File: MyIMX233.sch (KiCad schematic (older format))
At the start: 79 parts, among them IC1 iMX233, IC2 DDR_SDRAM_MT46_x16, J1 USB_OTG, P1 P4v2, P2 1v2, P3 VDDA1v8, P4 2v5, P5 3v3, P6 P4v2, SW1 SWITCH_PUSHBUTTON, Y1 24Mhz

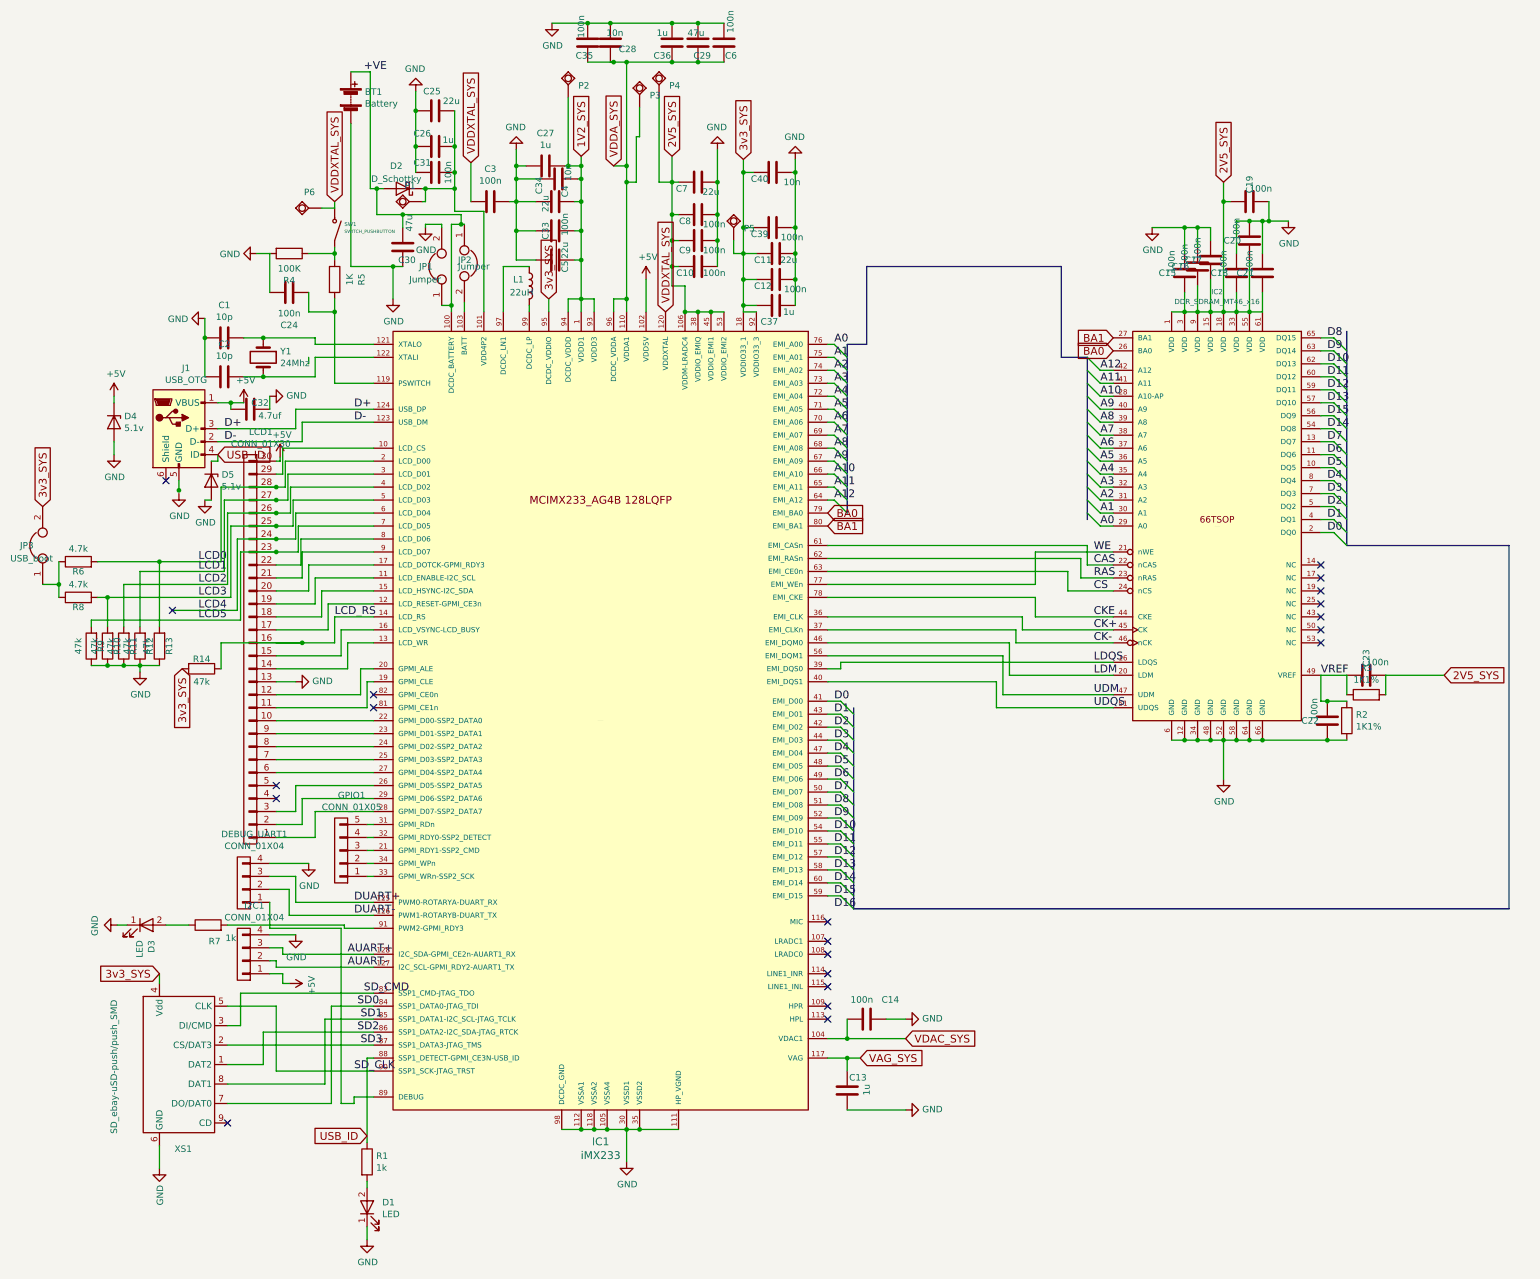
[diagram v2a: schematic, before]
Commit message: added boot resistors and 2.5v_VDDM is separated for ram, new battery connections with resistors for non battery mode
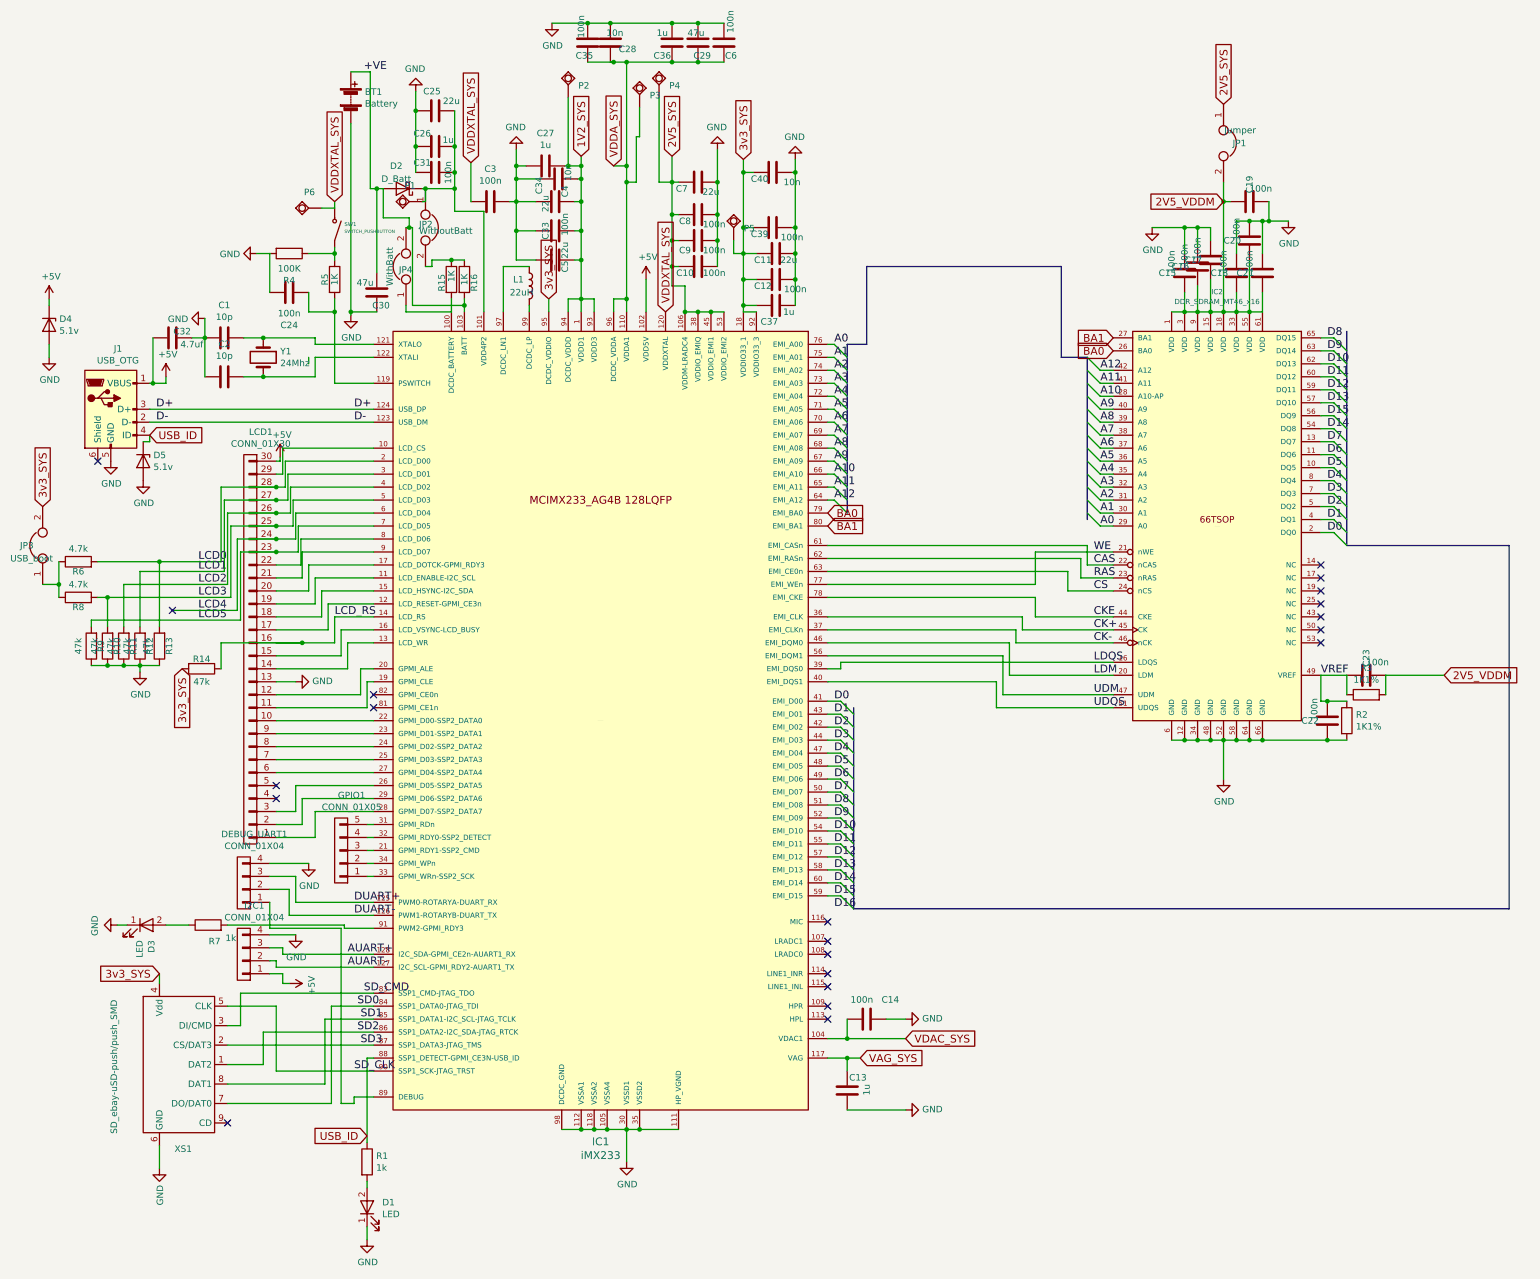
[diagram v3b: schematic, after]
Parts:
- added JP4: WithBatt, Pin_Headers:Pin_Header_Straight_1x02_Pitch2.54mm, symbol Jumper
- added R15, R16: 1K, Resistors_SMD:R_0603, symbol R
- D2: value D_Schottky -> D_Batt
- JP2: value Jumper -> WithoutBatt
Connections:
- net +VE: now also IC1.103 (BATT), JP4.2, R16.2; no longer IC1.100 (DCDC_BATTERY), JP1.1, JP2.1
- net 2V5_SYS: now also JP1.1; no longer C15.1, C16.1, C17.1, C18.1, C19.1, C20.1, C21.1, C23.2, IC2.1 (VDD), IC2.15 (VDD), IC2.18 (VDD), IC2.3 (VDD), IC2.33 (VDD), IC2.55 (VDD), IC2.61 (VDD), IC2.9 (VDD), R3.2
- net GND: now also J1.5 (GND); no longer JP1.2
- net at C25.2, C26.2, C31.1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: now also JP2.1
- net at JP2.2: now also R15.1, R16.1; no longer IC1.103 (BATT)
- new net: IC1.100 (DCDC_BATTERY), JP4.1, R15.2
- new net 2V5_VDDM: C15.1, C16.1, C17.1, C18.1, C19.1, C20.1, C21.1, C23.2, IC2.1 (VDD), IC2.15 (VDD), IC2.18 (VDD), IC2.3 (VDD), IC2.33 (VDD), IC2.55 (VDD), IC2.61 (VDD), IC2.9 (VDD), JP1.2, R3.2
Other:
- moved on the sheet: C30, C32, D4, D5, J1, JP1, JP2

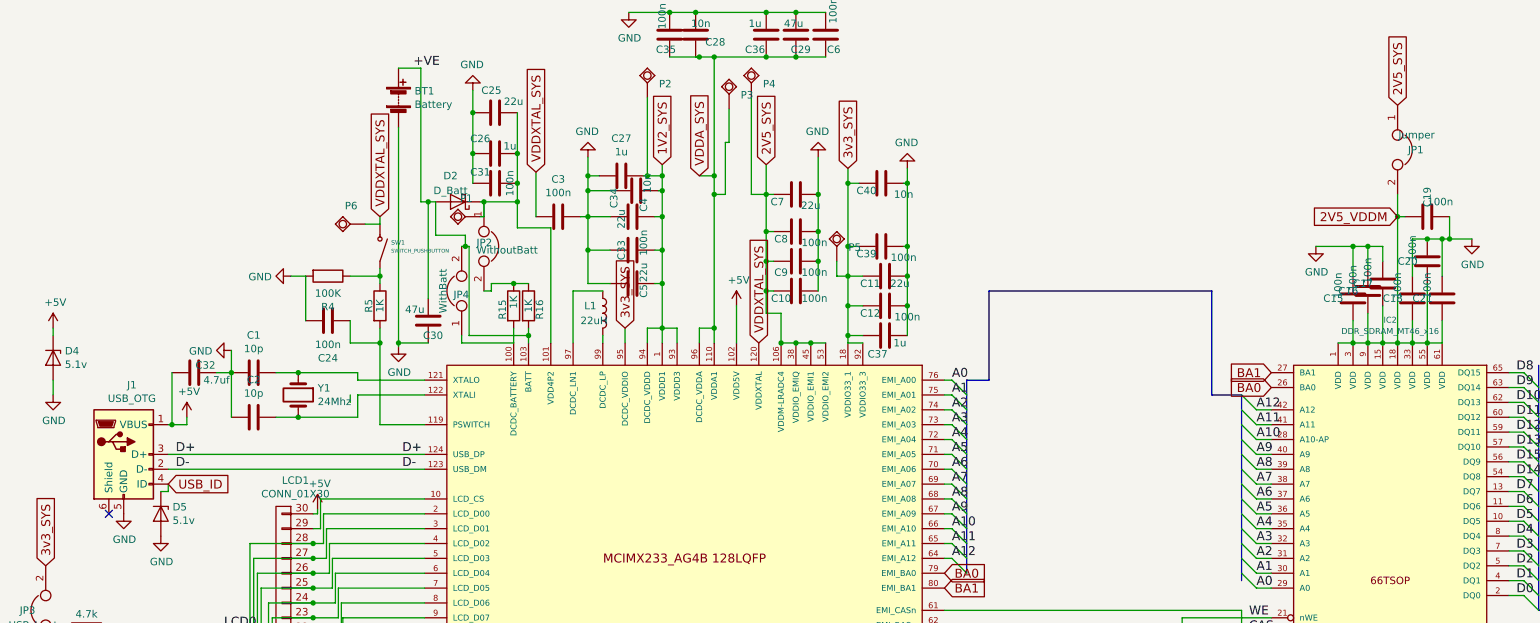
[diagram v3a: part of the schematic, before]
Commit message: resistors placement
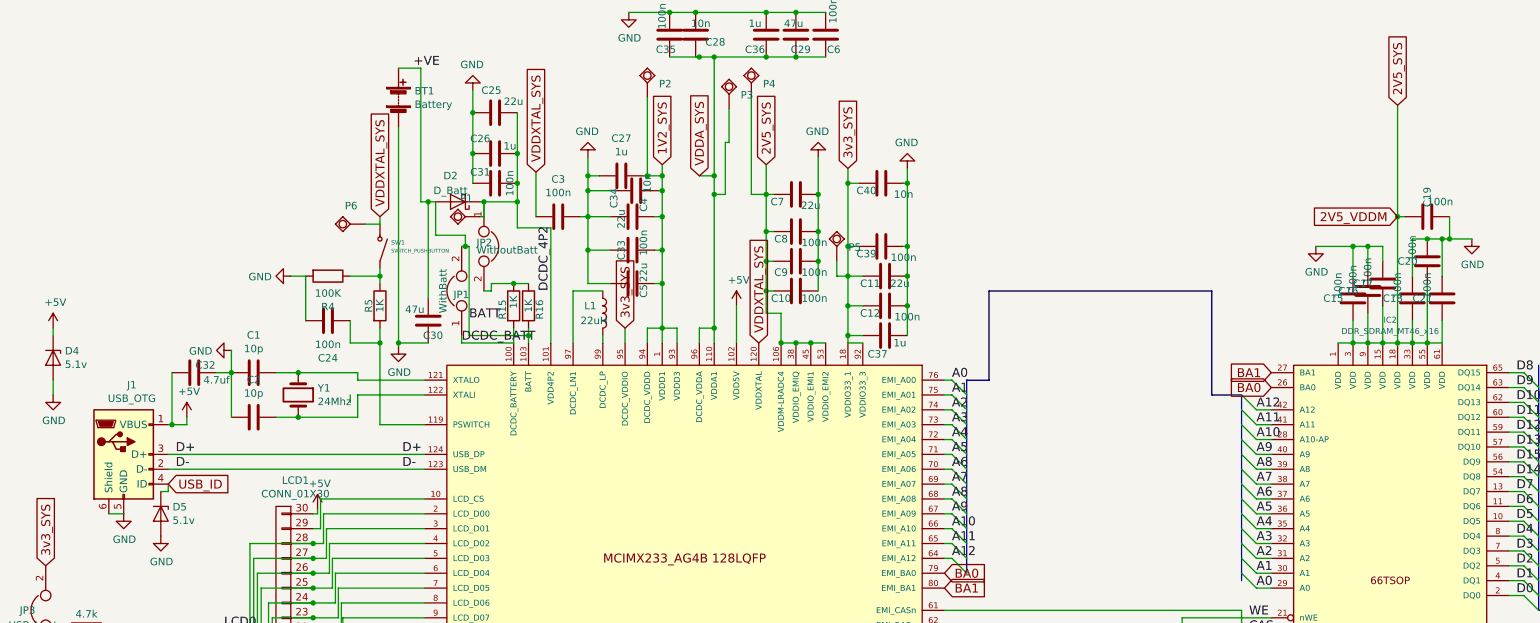
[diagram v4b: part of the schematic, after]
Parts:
- removed JP1: Jumper, Pin_Headers:Pin_Header_Straight_1x02_Pitch2.54mm, symbol Jumper
- renumbered JP4 to JP1
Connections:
- net 2V5_VDDM is gone; now on net 2V5_SYS: C15.1, C16.1, C17.1, C18.1, C19.1, C20.1, C21.1, C23.2, IC2.1 (VDD), IC2.15 (VDD), IC2.18 (VDD), IC2.3 (VDD), IC2.33 (VDD), IC2.55 (VDD), IC2.61 (VDD), IC2.9 (VDD), R3.2
- net GND: now also J1.6 (Shield)
- net DCDC_BATT: now reaches IC1.100 (DCDC_BATTERY), JP1.1, R15.2
- net DCDC_4P2: now reaches C25.2, C26.2, C31.1, D2.1 (K), IC1.101 (VDD4P2), JP2.1, P1.P$1 (PP)
- no-connect marks 21 -> 20
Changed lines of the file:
@@
 	1    0    0    -1
-$EndComp
-$Comp
-L Jumper JP1
-U 1 1 592F9D70
-P 9800 1450
-F 0 "JP1" V 9800 1625 50  0000 R CNN
-F 1 "Jumper" V 9700 1700 50  0000 R CNN
-F 2 "Pin_Headers:Pin_Header_Straight_1x02_Pitch2.54mm" H 9800 1450 50  0001 C CNN
-F 3 "" H 9800 1450 50  0001 C CNN
-	1    9800 1450
-	0    1    1    0
 $EndComp
 Text GLabel 4600 2650 1    60   Input ~ 0
@@
 	1    0    0    -1
 $EndComp
-NoConn ~ 1125 3900
 $Comp
 L R R14
@@
 Connection ~ 9500 2750
 Wire Wire Line
-	9800 1750 9800 2750
+	9800 1150 9800 2750
 Wire Wire Line
 	9800 1900 9850 1900
@@
 Connection ~ 3850 2350
 $Comp
-L Jumper JP4
+L Jumper JP1
 U 1 1 59974B70
 P 3500 2400
-F 0 "JP4" V 3475 2350 50  0000 L CNN
+F 0 "JP1" V 3475 2350 50  0000 L CNN
 F 1 "WithBatt" H 3350 2525 50  0000 L CNN
 F 2 "Pin_Headers:Pin_Header_Straight_1x02_Pitch2.54mm" H 3500 2400 50  0001 C CNN
@@
 	3275 2750 3075 2750
 Connection ~ 3075 2750
+Text Label 3500 2750 0    60   ~ 0
+DCDC_BATT
+Text Label 3550 2600 0    60   ~ 0
+BATT
+Text Label 4100 2400 1    60   ~ 0
+DCDC_4P2
+Wire Wire Line
+	1125 3900 1225 3900
 $EndSCHEMATC
